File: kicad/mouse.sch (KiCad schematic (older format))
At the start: 19 parts, among them IC1 L7805, P1 SOURCE_12v, P10 LED_CONN, P11 SW_CONN, P12 LED_K_CONN, P2 SOURCE_12v, P3 battery 12v, P4 SOURCE_5v, P5 SOURCE_5v, P6 SOURCE_5v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

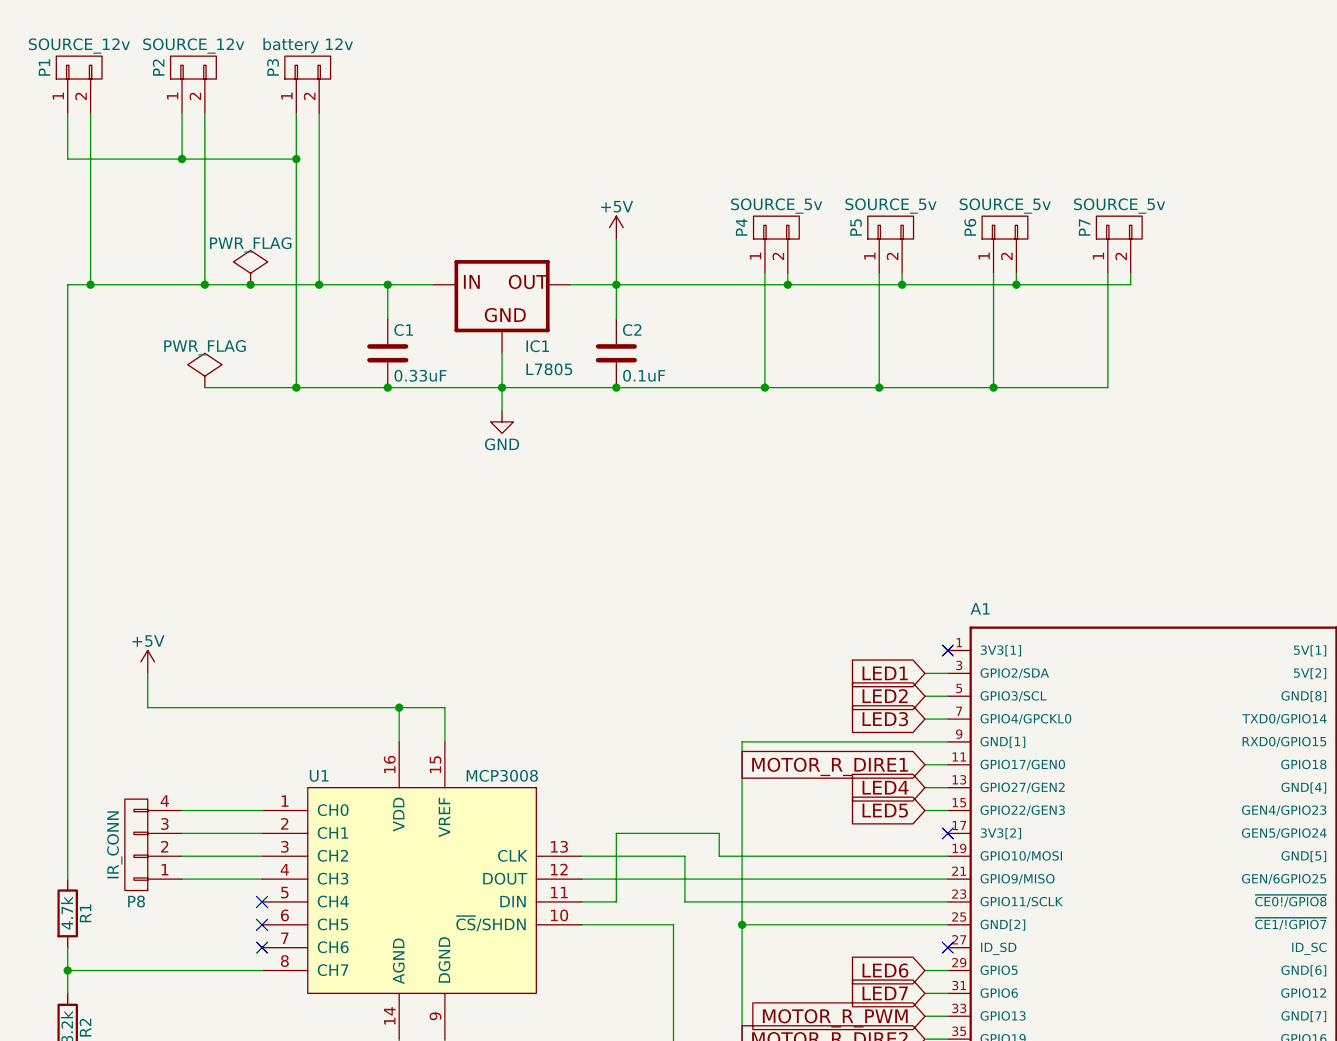
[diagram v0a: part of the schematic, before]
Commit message: add kicad
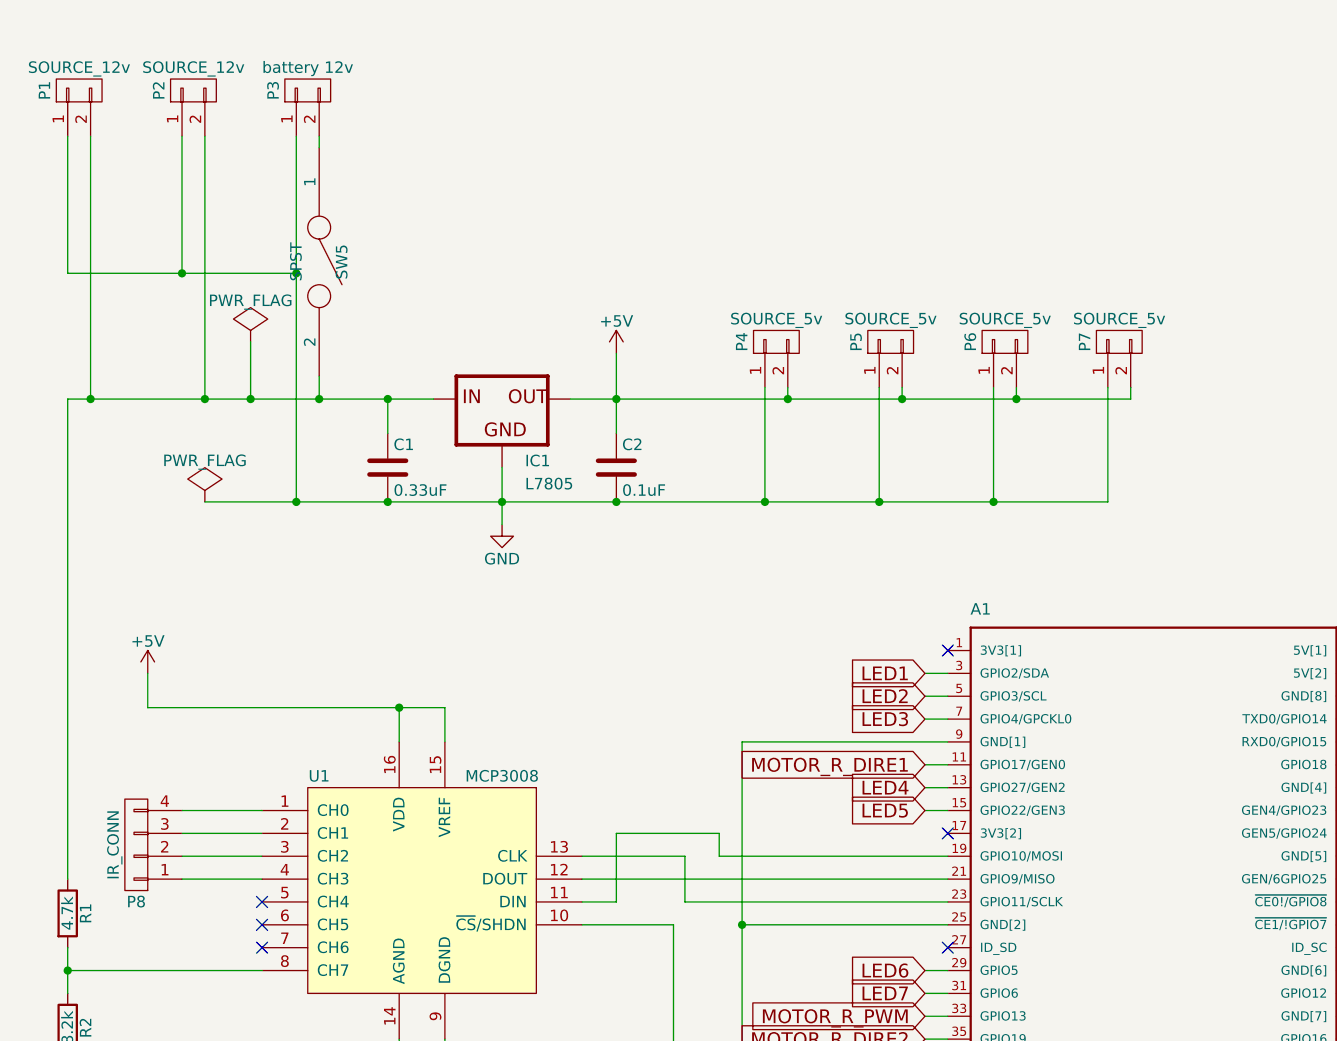
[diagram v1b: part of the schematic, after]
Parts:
- added SW5: SPST, Buttons_Switches_ThroughHole:SW_DIP_x1_Slide, symbol SPST
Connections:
- net at C1.1, IC1.IN, P1.2 (P2)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: now also SW5.2; no longer P3.2 (P2)
- new net: P3.2 (P2), SW5.1
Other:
- moved on the sheet: C1, C2, IC1, P1, P2, P3, P4, P5, P6, P7
